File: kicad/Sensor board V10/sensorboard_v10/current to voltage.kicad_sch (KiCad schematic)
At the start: 12 parts, among them J4 Conn_01x02, J5 Conn_01x02, J8 Conn_01x02, J9 Conn_01x02, U6 LM324

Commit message: Sensor Board V10 schematics
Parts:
- added C22, C23, C24, C25: 100nF, RMC_Capacitor:C_0805_2012Metric_Pad1.18x1.45mm_HandSolder_L, symbol Device:C
- added R30, R32, R34: 5k, RMC_Resistor:R_0805_2012Metric_Pad1.20x1.40mm_HandSolder_L, symbol Device:R
- added R31, R33, R35: 1k, RMC_Resistor:R_0805_2012Metric_Pad1.20x1.40mm_HandSolder_L, symbol Device:R
- R24, R25, R26, R27: footprint RMC_Resistor:R_0805_2012Metric_Pad1.20x1.40mm_HandSolder_L -> RMC_Resistor:R_1206_3216Metric_Pad1.30x1.75mm_HandSolder_RMC
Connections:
- net BRAKE_TEMP_OUT1: now also C22.1
- net BRAKE_TEMP_OUT2: now also C25.1, R30.2; no longer U6.9 (-)
- net BRAKE_TEMP_OUT3: now also C23.1, R32.2; no longer U6.6 (-)
- net BRAKE_TEMP_OUT4: now also C24.1, R34.2; no longer U6.13 (-)
- net GND: now also C22.2, C23.2, C24.2, C25.2, R31.1, R33.1, R35.1
- new net: R30.1, R31.2, U6.9 (-)
- new net: R34.1, R35.2, U6.13 (-)
- new net: R32.1, R33.2, U6.6 (-)
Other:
- moved on the sheet: C21, R24, R25, R26, R27, R28, R29, U6A, U6B, U6C, U6D, U6E

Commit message: Sensor Board v10
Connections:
- net BRAKE_TEMP1: now also J4.1 (Pin_1), U6.5 (+); no longer J4.2 (Pin_2), U6.3 (+)
- net BRAKE_TEMP2: now also J5.1 (Pin_1), U6.3 (+); no longer J5.2 (Pin_2), U6.10 (+)
- net BRAKE_TEMP3: now also J8.1 (Pin_1), U6.12 (+); no longer J8.2 (Pin_2), U6.5 (+)
- net BRAKE_TEMP4: now also J9.1 (Pin_1), U6.10 (+); no longer J9.2 (Pin_2), U6.12 (+)
- net BRAKE_TEMP_OUT1: now also U6.7; no longer U6.1
- net BRAKE_TEMP_OUT2: now also U6.1; no longer U6.8
- net BRAKE_TEMP_OUT3: now also U6.14; no longer U6.7
- net BRAKE_TEMP_OUT4: now also U6.8; no longer U6.14
- net GND: no longer J4.1 (Pin_1), J5.1 (Pin_1), J8.1 (Pin_1), J9.1 (Pin_1), R24.1, R25.1, R26.1, R27.1
- net at R28.1, R29.2: now also U6.6 (-); no longer U6.2 (-)
- net at R30.1, R31.2: now also U6.2 (-); no longer U6.9 (-)
- net at R34.1, R35.2: now also U6.9 (-); no longer U6.13 (-)
- net at R32.1, R33.2: now also U6.13 (-); no longer U6.6 (-)
- new net +24V: J4.2 (Pin_2), J5.2 (Pin_2), J8.2 (Pin_2), J9.2 (Pin_2)
- new net GND2: R24.1, R25.1, R26.1, R27.1
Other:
- moved on the sheet: C25, J4, J5, R26, U6A, U6B, U6C, U6D

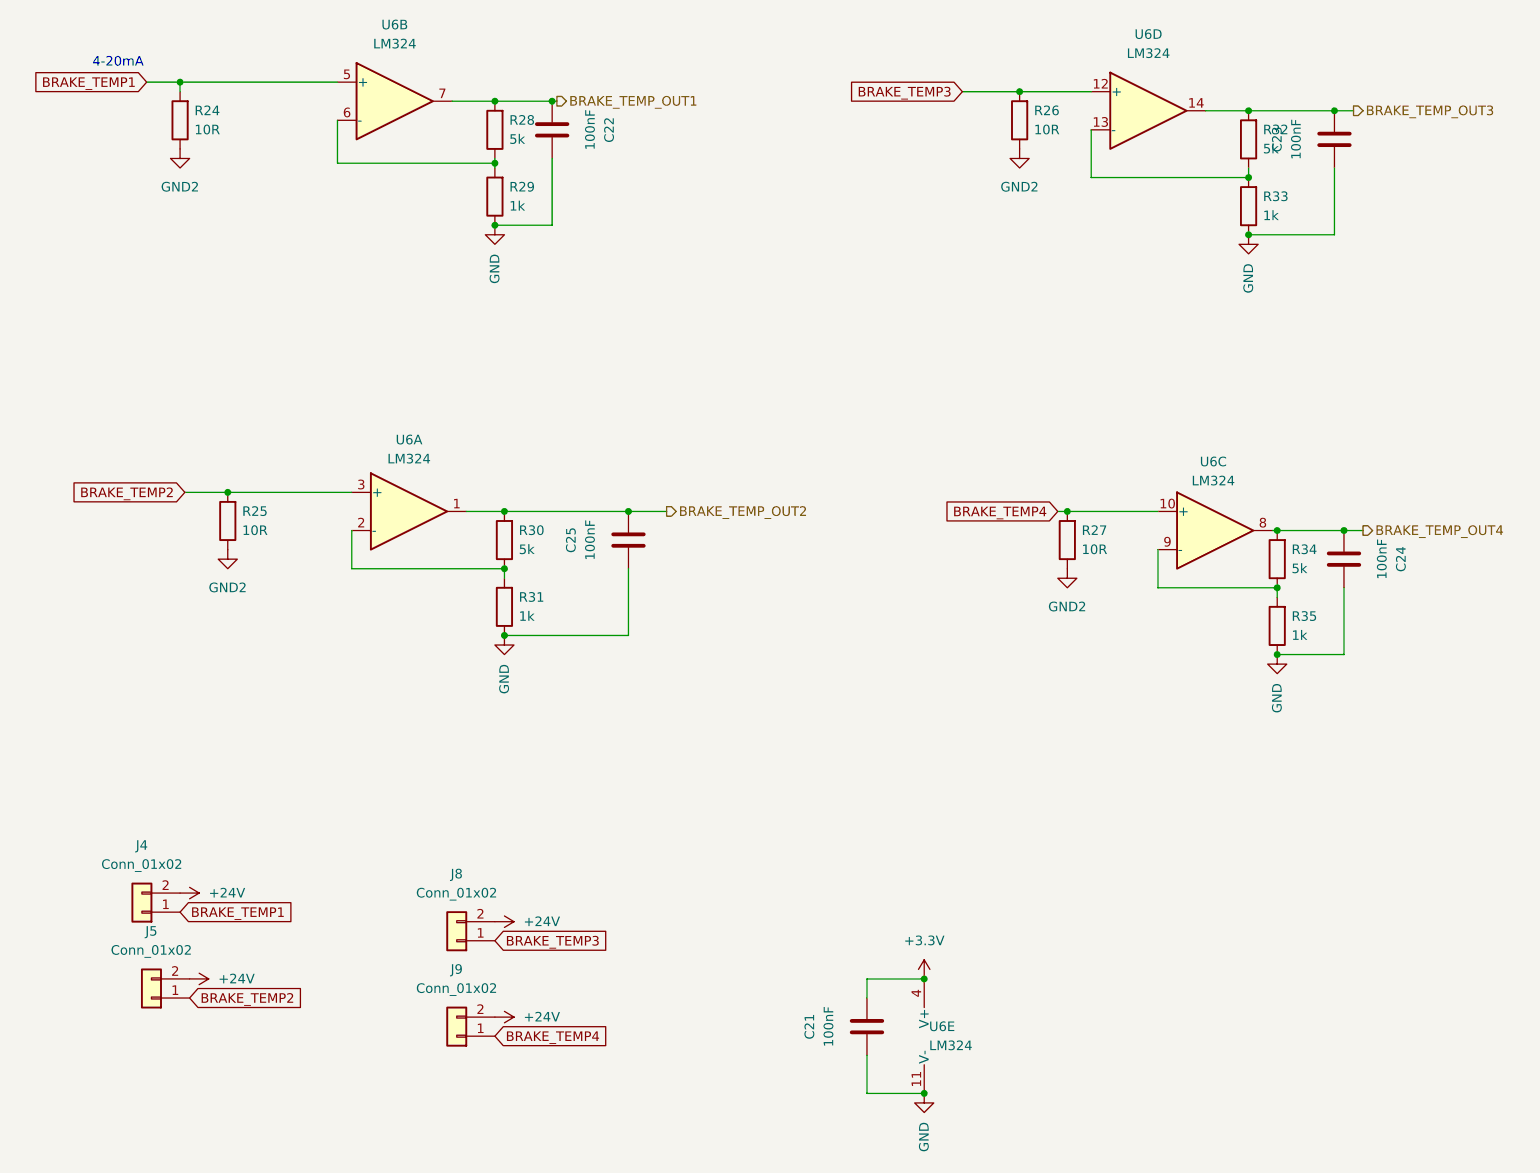
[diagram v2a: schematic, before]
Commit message: Sensor Board V10.0 done
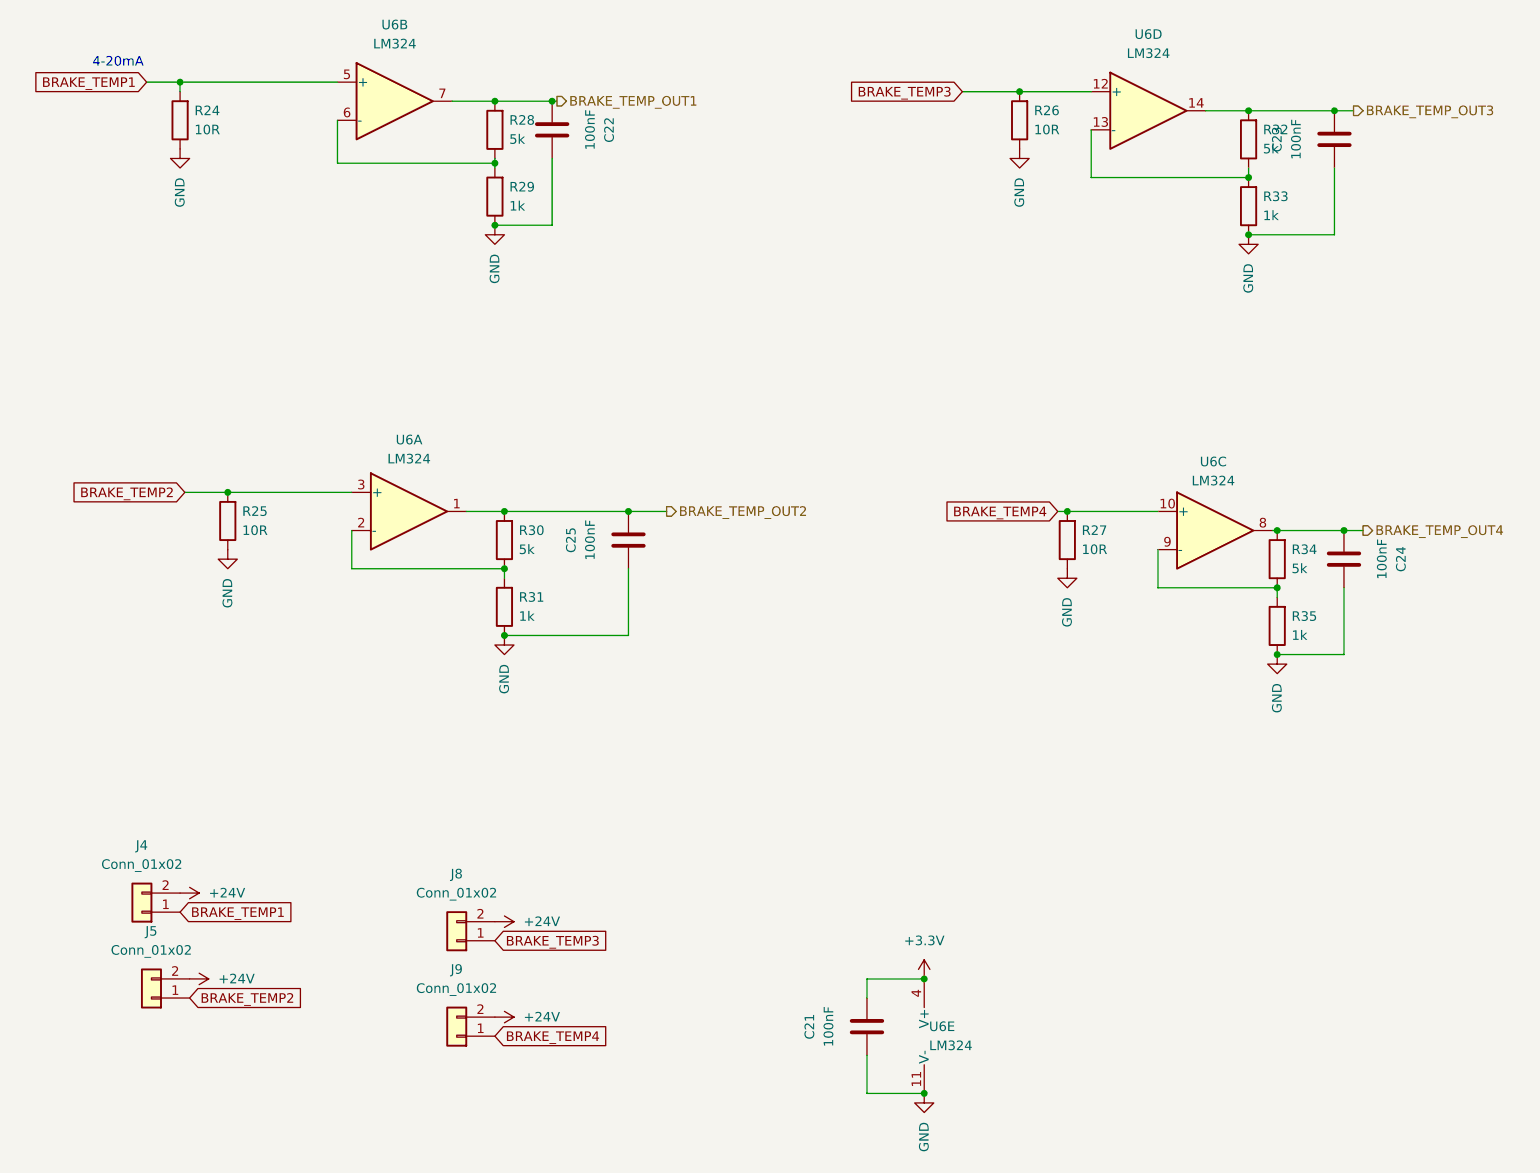
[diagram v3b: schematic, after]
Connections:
- net GND2 is gone; now on net GND: R24.1, R25.1, R26.1, R27.1
